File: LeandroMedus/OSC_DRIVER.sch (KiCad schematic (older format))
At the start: 0 parts

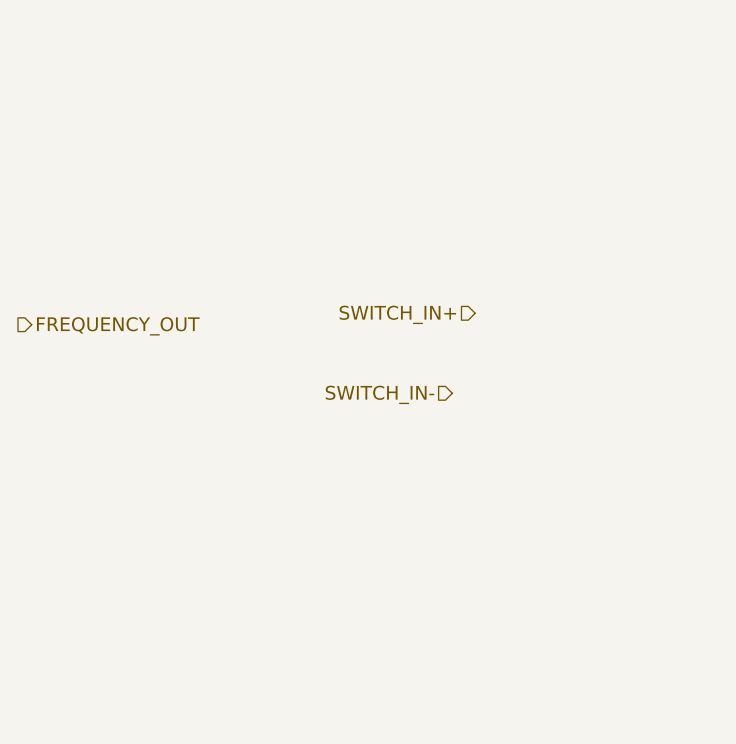
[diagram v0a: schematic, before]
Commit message: Fin clase 2 faltante
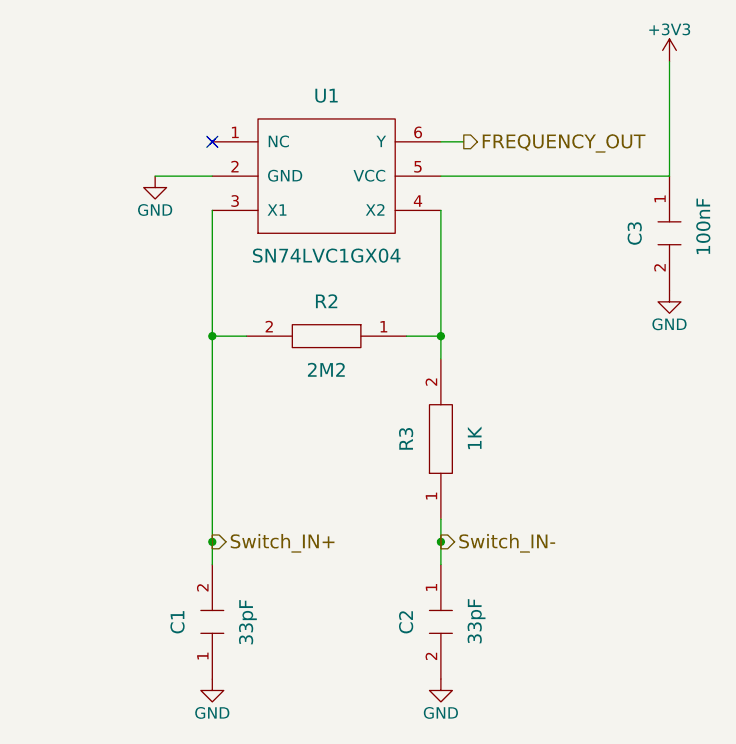
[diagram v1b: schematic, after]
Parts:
- added C1, C2: 33pF, OpenQCM:C_0805_HandSoldering, symbol Capacitor_SMD_HandSoldering
- added C3: 100nF, OpenQCM:C_0805_HandSoldering, symbol Capacitor_SMD_HandSoldering
- added R2: 2M2, OpenQCM:R_0805_HandSoldering, symbol Resistor_0805_HandSoldering
- added R3: 1K, OpenQCM:R_0805_HandSoldering, symbol Resistor_0805_HandSoldering
- added U1: SN74LVC1GX04, OpenQCM:SOT-23-6, symbol SN74LVC1GX04
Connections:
- net FREQUENCY_OUT: now also U1.6 (Y)
- new net: R2.1, R3.2, U1.4 (X2)
- new net +3V3: C3.1, U1.5 (VCC)
- new net GND: C1.1, C2.2, C3.2, U1.2 (GND)
- new net Switch_IN+: C1.2, R2.2, U1.3 (X1)
- new net Switch_IN-: C2.1, R3.1
- no-connect marks 0 -> 1
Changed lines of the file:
@@
 encoding utf-8
 Sheet 3 4
-Title "Ejercicio n° 2"
-Date "2016-03-28"
-Rev "0.1"
-Comp "FI-UNER"
-Comment1 "Pruebas correspondientes al curso de KiCad"
+Title "OpenQCM Diss"
+Date "2016-02-04"
+Rev "2.1"
+Comp "UNER"
+Comment1 ""
 Comment2 ""
 Comment3 ""
 Comment4 ""
 $EndDescr
-Text HLabel 4250 2600 2    60   Output ~ 0
+$Comp
+L SN74LVC1GX04 U1
+U 1 1 56E7582E
+P 5600 1950
+F 0 "U1" H 5600 2300 60  0000 C CNN
+F 1 "SN74LVC1GX04" H 5600 1600 60  0000 C CNN
+F 2 "OpenQCM:SOT-23-6" H 5600 1950 60  0001 C CNN
+F 3 "" H 5600 1950 60  0000 C CNN
+F 4 "Value" H 5600 1950 60  0001 C CNN "Digikey/Mouser"
+	1    5600 1950
+	1    0    0    -1
+$EndComp
+$Comp
+L +3V3 #PWR010
+U 1 1 56E75836
+P 7100 1450
+F 0 "#PWR010" H 7100 1300 50  0001 C CNN
+F 1 "+3V3" H 7100 1590 50  0000 C CNN
+F 2 "" H 7100 1450 60  0000 C CNN
+F 3 "" H 7100 1450 60  0000 C CNN
+	1    7100 1450
+	1    0    0    -1
+$EndComp
+Wire Wire Line
+	6100 1800 6200 1800
+Wire Wire Line
+	6100 1950 7100 1950
+Wire Wire Line
+	7100 1950 7100 1450
+NoConn ~ 5100 1800
+$Comp
+L GND #PWR011
+U 1 1 56E75840
+P 4850 1950
+F 0 "#PWR011" H 4850 1700 50  0001 C CNN
+F 1 "GND" H 4850 1800 50  0000 C CNN
+F 2 "" H 4850 1950 60  0000 C CNN
+F 3 "" H 4850 1950 60  0000 C CNN
+	1    4850 1950
+	1    0    0    -1
+$EndComp
+Wire Wire Line
+	5100 1950 4850 1950
+$Comp
+L Capacitor_SMD_HandSoldering C3
+U 1 1 56E75848
+P 7100 2200
+F 0 "C3" H 7100 2350 60  0000 C CNN
+F 1 "100nF" H 7200 2050 60  0000 R CNN
+F 2 "OpenQCM:C_0805_HandSoldering" H 7100 2200 60  0001 C CNN
+F 3 "" H 7100 2200 60  0000 C CNN
+F 4 "Value" H 7100 2200 60  0001 C CNN "Digikey/Mouser"
+	1    7100 2200
+	0    -1   1    0
+$EndComp
+$Comp
+L GND #PWR012
+U 1 1 56E7584F
+P 7100 2450
+F 0 "#PWR012" H 7100 2200 50  0001 C CNN
+F 1 "GND" H 7100 2300 50  0000 C CNN
+F 2 "" H 7100 2450 60  0000 C CNN
+F 3 "" H 7100 2450 60  0000 C CNN
+	1    7100 2450
+	1    0    0    -1
+$EndComp
+Wire Wire Line
+	7100 2450 7100 2450
+$Comp
+L Resistor_0805_HandSoldering R2
+U 1 1 56E75857
+P 5600 2650
+F 0 "R2" H 5600 2800 60  0000 C CNN
+F 1 "2M2" H 5600 2500 60  0000 C CNN
+F 2 "OpenQCM:R_0805_HandSoldering" H 5600 2650 60  0001 C CNN
+F 3 "" H 5600 2650 60  0000 C CNN
+F 4 "Value" H 5600 2650 60  0001 C CNN "Digikey/Mouser"
+	1    5600 2650
+	-1   0    0    -1
+$EndComp
+$Comp
+L Resistor_0805_HandSoldering R3
+U 1 1 56E7585F
+P 6100 3100
+F 0 "R3" H 6100 3250 60  0000 C CNN
+F 1 "1K" H 6100 2950 60  0000 C CNN
+F 2 "OpenQCM:R_0805_HandSoldering" H 6100 3100 60  0001 C CNN
+F 3 "" H 6100 3100 60  0000 C CNN
+F 4 "Value" H 6100 3100 60  0001 C CNN "Digikey/Mouser"
+	1    6100 3100
+	0    -1   -1   0
+$EndComp
+$Comp
+L Capacitor_SMD_HandSoldering C1
+U 1 1 56E75867
+P 5100 3900
+F 0 "C1" H 5100 4050 60  0000 C CNN
+F 1 "33pF" H 5200 3750 60  0000 R CNN
+F 2 "OpenQCM:C_0805_HandSoldering" H 5100 3900 60  0001 C CNN
+F 3 "" H 5100 3900 60  0000 C CNN
+F 4 "Value" H 5100 3900 60  0001 C CNN "Digikey/Mouser"
+	1    5100 3900
+	0    -1   -1   0
+$EndComp
+$Comp
+L Capacitor_SMD_HandSoldering C2
+U 1 1 56E7586F
+P 6100 3900
+F 0 "C2" H 6100 4050 60  0000 C CNN
+F 1 "33pF" H 6200 3750 60  0000 R CNN
+F 2 "OpenQCM:C_0805_HandSoldering" H 6100 3900 60  0001 C CNN
+F 3 "" H 6100 3900 60  0000 C CNN
+F 4 "Value" H 6100 3900 60  0001 C CNN "Digikey/Mouser"
+	1    6100 3900
+	0    -1   1    0
+$EndComp
+$Comp
+L GND #PWR013
+U 1 1 56E75876
+P 5100 4150
+F 0 "#PWR013" H 5100 3900 50  0001 C CNN
+F 1 "GND" H 5100 4000 50  0000 C CNN
+F 2 "" H 5100 4150 60  0000 C CNN
+F 3 "" H 5100 4150 60  0000 C CNN
+	1    5100 4150
+	1    0    0    -1
+$EndComp
+$Comp
+L GND #PWR014
+U 1 1 56E7587C
+P 6100 4150
+F 0 "#PWR014" H 6100 3900 50  0001 C CNN
+F 1 "GND" H 6100 4000 50  0000 C CNN
+F 2 "" H 6100 4150 60  0000 C CNN
+F 3 "" H 6100 4150 60  0000 C CNN
+	1    6100 4150
+	1    0    0    -1
+$EndComp
+Wire Wire Line
+	5950 2650 6100 2650
+Wire Wire Line
+	6100 2100 6100 2750
+Connection ~ 6100 2650
+Wire Wire Line
+	5250 2650 5100 2650
+Wire Wire Line
+	5100 2100 5100 3650
+Wire Wire Line
+	6100 3450 6100 3650
+Connection ~ 5100 2650
+Connection ~ 6100 3550
+Connection ~ 5100 3550
+Text HLabel 5100 3550 2    60   Output ~ 0
+Switch_IN+
+Text HLabel 6100 3550 2    60   Output ~ 0
+Switch_IN-
+Text HLabel 6200 1800 2    60   Output ~ 0
 FREQUENCY_OUT
-Text HLabel 6250 2550 0    60   Input ~ 0
-SWITCH_IN+
-Text HLabel 6150 2900 0    60   Input ~ 0
-SWITCH_IN-
 $EndSCHEMATC
